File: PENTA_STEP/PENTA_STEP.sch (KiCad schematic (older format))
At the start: 121 parts, among them J1 DB25_Female_LCNC, J10 ENC_HEADER, J11 ENC_HEADER, J12 PSoC_PROG, J13 PWR_SW_CH1, J14 SCREW TERM, J15 SCREW TERM, J16 ENC_HEADER, J17 ENC_HEADER, J18 SCREW TERM, J19 SCREW TERM, J2 MTA-100, J20 CYP_I2C, J21 PWR_SW_CH2, J3 USB_B, J4 SPARE_IN, J5 ENC_HEADER, J7 CYP_GPIO, J9 SCREW TERM, Q21 AON7804, U2 CY8C5468AXI-LP106

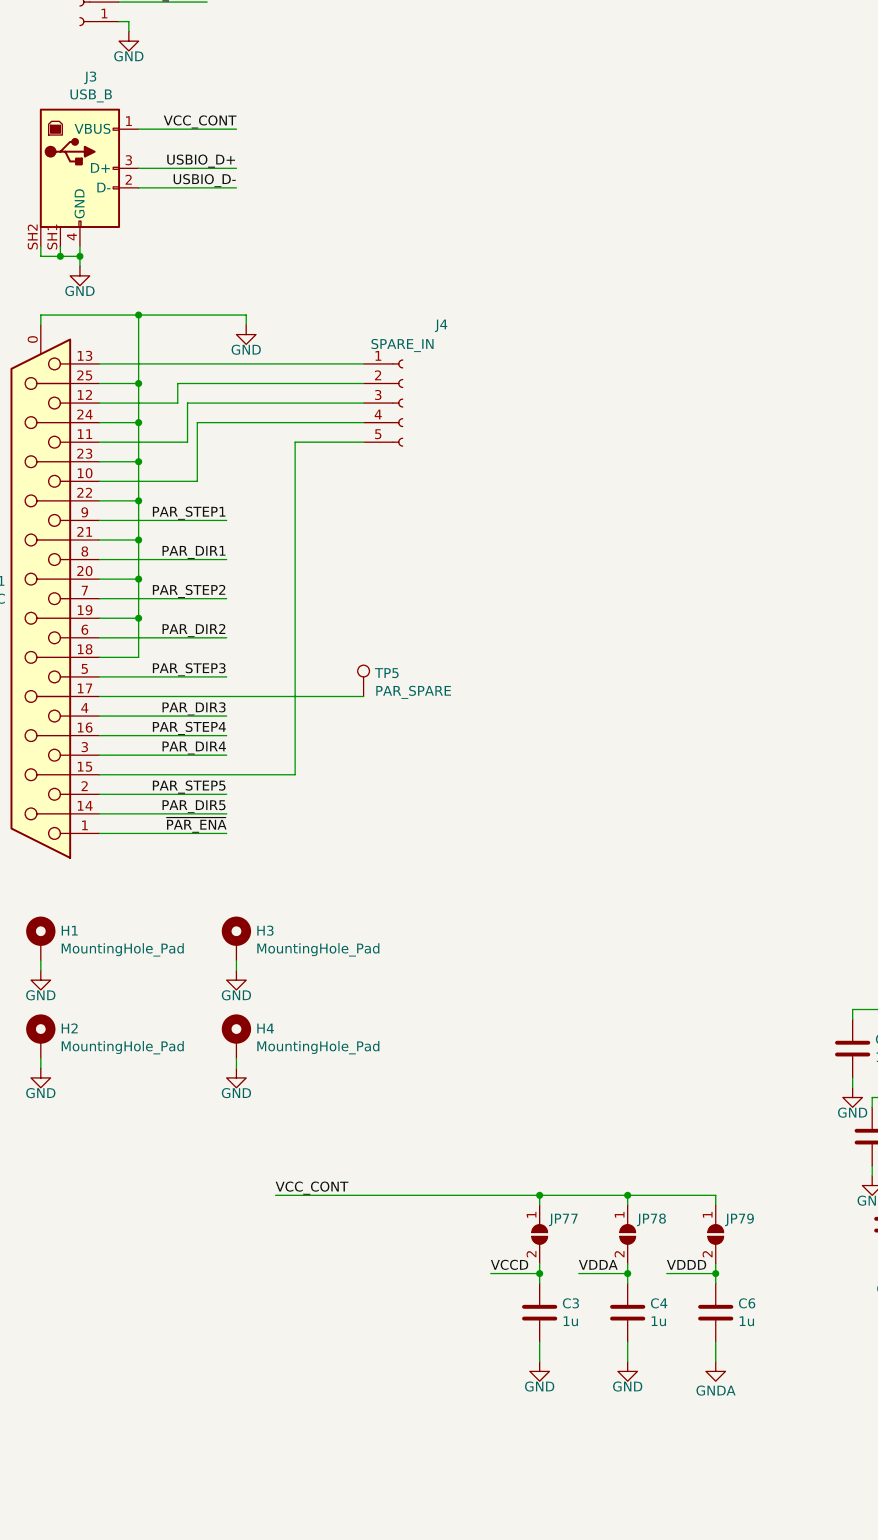
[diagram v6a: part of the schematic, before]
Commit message: finalized BOM, found TMC5160-TA being replaced by TMC5160A-TA
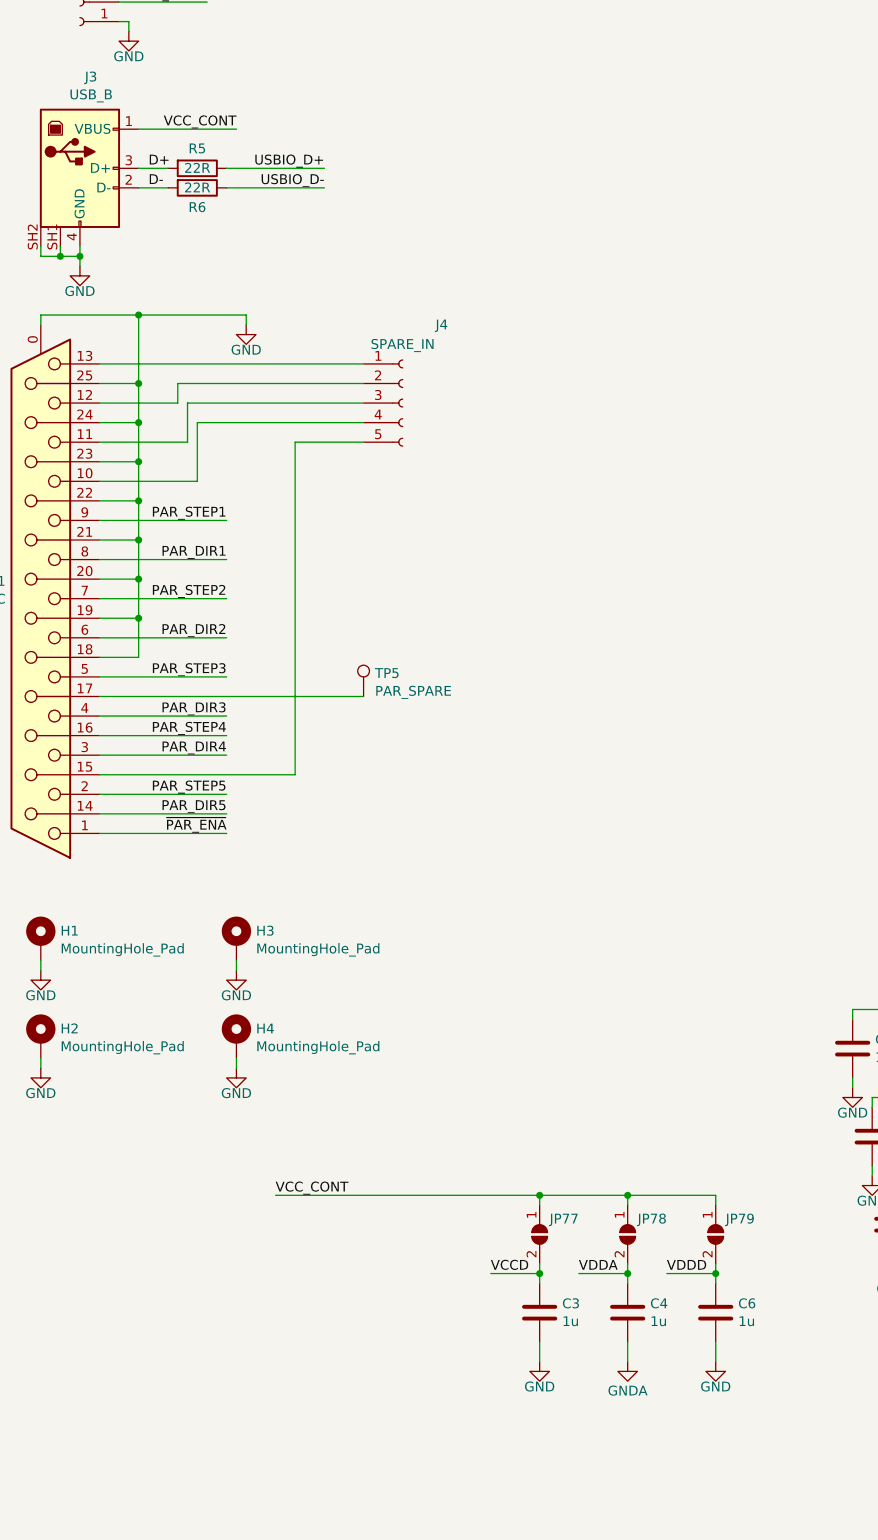
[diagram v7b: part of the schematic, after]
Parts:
- added R5, R6: 22R, Resistor_SMD:R_0603_1608Metric_Pad1.05x0.95mm_HandSolder, symbol Device:R
- J10, J11, J16, J17, J5: DPN (none) -> HDR100MET40M-G-RA-TH-ND; MPN (none) -> HDR100MET40M-G-RA-TH
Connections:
- net GND: now also C6.2; no longer C4.2
- net GNDA: now also C4.2; no longer C6.2
- net USBIO_D+: now also R5.1; no longer J3.3 (D+)
- net USBIO_D-: now also R6.1; no longer J3.2 (D-)
- new net D+: J3.3 (D+), R5.2
- new net D-: J3.2 (D-), R6.2
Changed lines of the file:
@@
 EESchema Schematic File Version 4
-LIBS:PENTA_STEP-cache
-EELAYER 26 0
+EELAYER 30 0
 EELAYER END
 $Descr A2 23386 16535
@@
 L power:GND #PWR07
 U 1 1 5EA1E77E
-P 4750 11950
-F 0 "#PWR07" H 4750 11700 50  0001 C CNN
-F 1 "GND" H 4750 11850 50  0000 C TNN
-F 2 "" H 4750 11950 50  0001 C CNN
-F 3 "" H 4750 11950 50  0001 C CNN
-	1    4750 11950
+P 5200 11950
+F 0 "#PWR07" H 5200 11700 50  0001 C CNN
+F 1 "GND" H 5200 11850 50  0000 C TNN
+F 2 "" H 5200 11950 50  0001 C CNN
+F 3 "" H 5200 11950 50  0001 C CNN
+	1    5200 11950
 	1    0    0    -1
 $EndComp
@@
 L power:GNDA #PWR09
 U 1 1 5EA20FAC
-P 5200 11950
-F 0 "#PWR09" H 5200 11700 50  0001 C CNN
-F 1 "GNDA" H 5200 11800 50  0000 C CNN
-F 2 "" H 5200 11950 50  0001 C CNN
-F 3 "" H 5200 11950 50  0001 C CNN
-	1    5200 11950
+P 4750 11950
+F 0 "#PWR09" H 4750 11700 50  0001 C CNN
+F 1 "GNDA" H 4750 11800 50  0000 C CNN
+F 2 "" H 4750 11950 50  0001 C CNN
+F 3 "" H 4750 11950 50  0001 C CNN
+	1    4750 11950
 	1    0    0    -1
 $EndComp
@@
 Wire Wire Line
 	10100 11850 9750 11850
-Text Label 2750 5850 2    50   ~ 0
+Text Label 3200 5850 2    50   ~ 0
 USBIO_D+
-Text Label 2750 5950 2    50   ~ 0
+Text Label 3200 5950 2    50   ~ 0
 USBIO_D-
 Wire Wire Line
-	2750 5850 2250 5850
+	3200 5850 2700 5850
 Wire Wire Line
-	2250 5950 2750 5950
+	2700 5950 3200 5950
 Wire Wire Line
 	10100 7450 9750 7450
@@
 F 2 "Connector_PinHeader_1.00mm:PinHeader_1x04_P1.00mm_Vertical" H 11600 3700 50  0001 C CNN
 F 3 "~" H 11600 3700 50  0001 C CNN
+F 4 "HDR100MET40M-G-RA-TH" H 11600 3700 50  0001 C CNN "MPN"
+F 5 "HDR100MET40M-G-RA-TH-ND" H 11600 3700 50  0001 C CNN "DPN"
 	1    11600 3700
 	-1   0    0    -1
@@
 F 2 "Connector_PinHeader_1.00mm:PinHeader_1x04_P1.00mm_Vertical" H 11600 6250 50  0001 C CNN
 F 3 "~" H 11600 6250 50  0001 C CNN
+F 4 "HDR100MET40M-G-RA-TH" H 11600 6250 50  0001 C CNN "MPN"
+F 5 "HDR100MET40M-G-RA-TH-ND" H 11600 6250 50  0001 C CNN "DPN"
 	1    11600 6250
 	-1   0    0    -1
@@
 F 2 "Connector_PinHeader_1.00mm:PinHeader_1x04_P1.00mm_Vertical" H 16500 6250 50  0001 C CNN
 F 3 "~" H 16500 6250 50  0001 C CNN
+F 4 "HDR100MET40M-G-RA-TH" H 16500 6250 50  0001 C CNN "MPN"
+F 5 "HDR100MET40M-G-RA-TH-ND" H 16500 6250 50  0001 C CNN "DPN"
 	1    16500 6250
 	-1   0    0    -1
@@
 F 2 "Connector_PinHeader_1.00mm:PinHeader_1x04_P1.00mm_Vertical" H 16500 3700 50  0001 C CNN
 F 3 "~" H 16500 3700 50  0001 C CNN
+F 4 "HDR100MET40M-G-RA-TH" H 16500 3700 50  0001 C CNN "MPN"
+F 5 "HDR100MET40M-G-RA-TH-ND" H 16500 3700 50  0001 C CNN "DPN"
 	1    16500 3700
 	-1   0    0    -1
@@
 F 2 "Connector_PinHeader_1.00mm:PinHeader_1x04_P1.00mm_Vertical" H 13650 9550 50  0001 C CNN
 F 3 "~" H 13650 9550 50  0001 C CNN
+F 4 "HDR100MET40M-G-RA-TH" H 13650 9550 50  0001 C CNN "MPN"
+F 5 "HDR100MET40M-G-RA-TH-ND" H 13650 9550 50  0001 C CNN "DPN"
 	1    13650 9550
 	-1   0    0    -1
@@
 	0    -1   1    0
 $EndComp
+$Comp
+L Device:R R5
+U 1 1 5E5936B2
+P 2550 5850
+AR Path="/5E5936B2" Ref="R5"  Part="1"
+AR Path="/5E4B7A4F/5E5936B2" Ref="R?"  Part="1"
+AR Path="/5E50A85F/5E5936B2" Ref="R?"  Part="1"
+AR Path="/5E50B0AB/5E5936B2" Ref="R?"  Part="1"
+AR Path="/5E50B60F/5E5936B2" Ref="R?"  Part="1"
+AR Path="/5F24B60D/5E5936B2" Ref="R?"  Part="1"
+F 0 "R5" V 2450 5850 50  0000 C CNN
+F 1 "22R" V 2550 5850 50  0000 C CNN
+F 2 "Resistor_SMD:R_0603_1608Metric_Pad1.05x0.95mm_HandSolder" V 2480 5850 50  0001 C CNN
+F 3 "~" H 2550 5850 50  0001 C CNN
+F 4 "ERJ-3EKF22R0V" H 2550 5850 50  0001 C CNN "MPN"
+F 5 "P22.0HCT-ND" H 2550 5850 50  0001 C CNN "DPN"
+F 6 "CRGCQ0603J22R,A130081CT-ND" V 2550 5850 50  0001 C CNN "ALTERNATE"
+	1    2550 5850
+	0    1    1    0
+$EndComp
+$Comp
+L Device:R R6
+U 1 1 5E608527
+P 2550 5950
+AR Path="/5E608527" Ref="R6"  Part="1"
+AR Path="/5E4B7A4F/5E608527" Ref="R?"  Part="1"
+AR Path="/5E50A85F/5E608527" Ref="R?"  Part="1"
+AR Path="/5E50B0AB/5E608527" Ref="R?"  Part="1"
+AR Path="/5E50B60F/5E608527" Ref="R?"  Part="1"
+AR Path="/5F24B60D/5E608527" Ref="R?"  Part="1"
+F 0 "R6" V 2650 5950 50  0000 C CNN
+F 1 "22R" V 2550 5950 50  0000 C CNN
+F 2 "Resistor_SMD:R_0603_1608Metric_Pad1.05x0.95mm_HandSolder" V 2480 5950 50  0001 C CNN
+F 3 "~" H 2550 5950 50  0001 C CNN
+F 4 "ERJ-3EKF22R0V" H 2550 5950 50  0001 C CNN "MPN"
+F 5 "P22.0HCT-ND" H 2550 5950 50  0001 C CNN "DPN"
+F 6 "CRGCQ0603J22R,A130081CT-ND" V 2550 5950 50  0001 C CNN "ALTERNATE"
+	1    2550 5950
+	0    1    1    0
+$EndComp
+Wire Wire Line
+	2250 5850 2400 5850
+Wire Wire Line
+	2400 5950 2250 5950
+Text Label 2300 5850 0    50   ~ 0
+D+
+Text Label 2300 5950 0    50   ~ 0
+D-
 $EndSCHEMATC
